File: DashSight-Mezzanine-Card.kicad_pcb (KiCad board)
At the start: 4 copper layers, 72 x 78.5 mm, 74 parts, among them IC2 ELM327, J1 Pi2 Connector, J2 Euler Connector, J3 Conn_Coaxial, J4 OBD2-DB9_Male, J5 Conn_02x05_Odd_Even, Q1 2N3904, Q2 2N3906, Q3 2N3906, Q4 2N3904, Q5 2N3904, Q6 2N3904, Q7 2N3904, SW1 SW_Push, SW2 SW_Push, U1 MCP2561-E/P, U2 LM317L_TO92, U3 LP2950-3.0_TO92, U4 ADuM1201AR, U5 NEO-M9N, Y1 4.0MHz

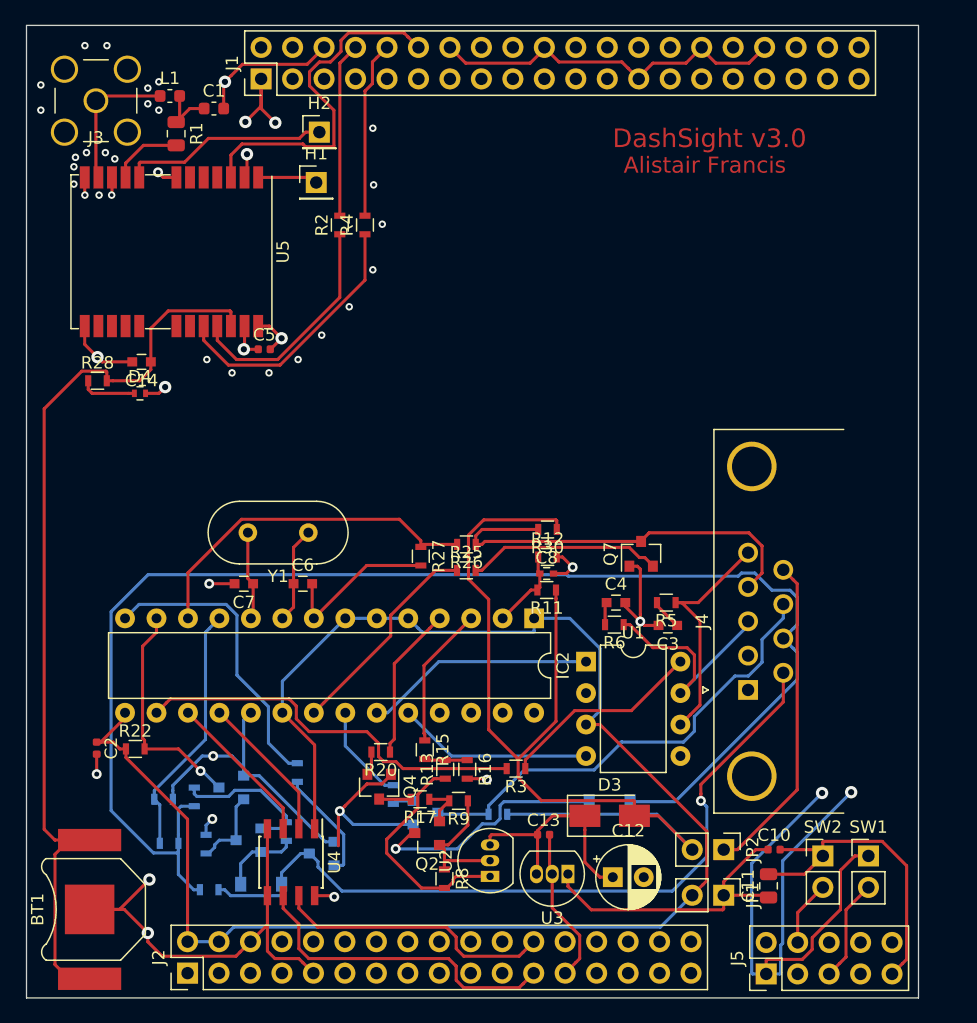
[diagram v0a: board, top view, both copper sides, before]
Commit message: pcb: Connect the IMU, GNSS PPS, Qwiic and other changes
Signed-off-by: Alistair Francis <alistair@alistair23.me>
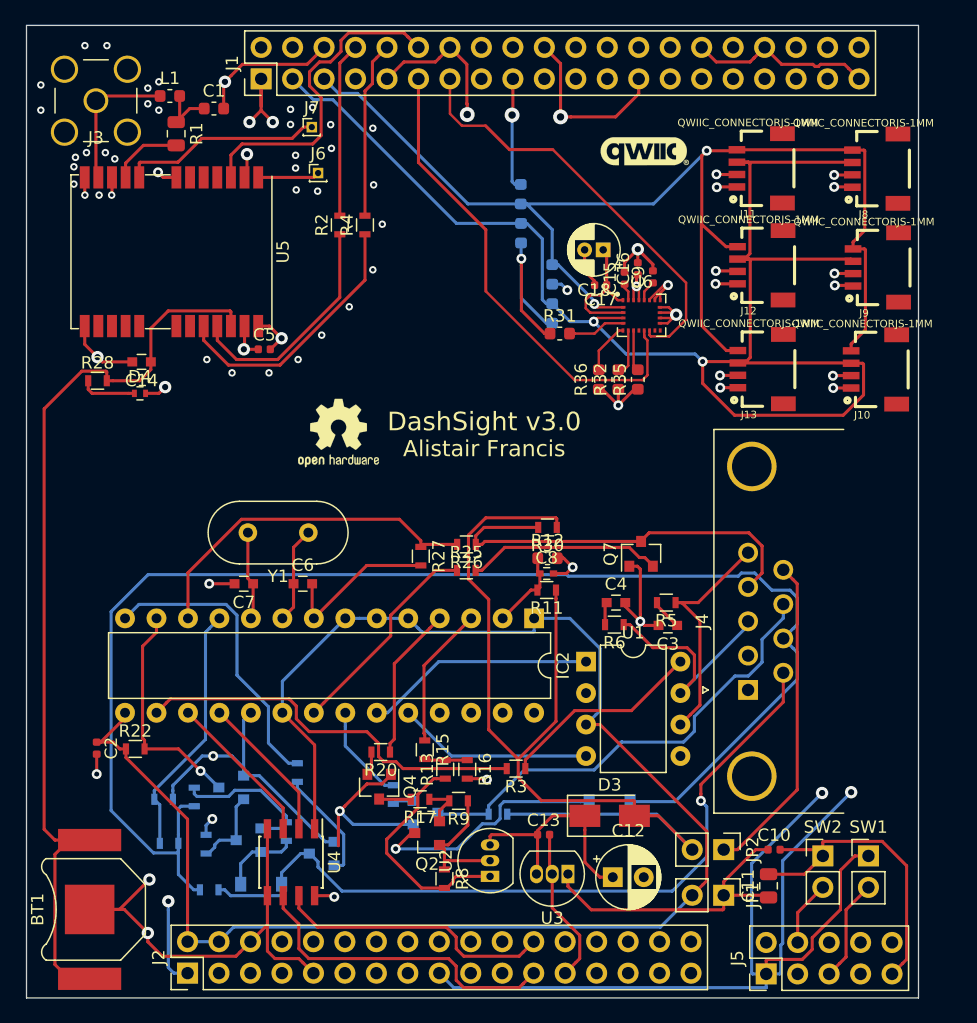
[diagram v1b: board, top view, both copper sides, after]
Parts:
- removed H1: Safeboot, Connector_PinHeader_2.54mm:PinHeader_1x01_P2.54mm_Vertical
- removed H2: Reset, Connector_PinHeader_2.54mm:PinHeader_1x01_P2.54mm_Vertical
- added C15: 0.1uF, Capacitor_SMD:C_0402_1005Metric, F.Cu at (176.3, 66.9)
- added C16: 0.1uF, Capacitor_SMD:C_0402_1005Metric, F.Cu at (177.3, 66.1)
- added C17: 0.1uF, Capacitor_SMD:C_0402_1005Metric, F.Cu at (174.3, 67.5)
- added C18: 10uF, Capacitor_THT:CP_Radial_D4.0mm_P1.50mm, F.Cu at (174.5, 64.6)
- added C9: 10nF (16V), Capacitor_SMD:C_0402_1005Metric, F.Cu at (178.6, 66.8)
- added G***: LOGO, DashSight:qwiic_logo, F.Cu at (177.9, 56.6)
- added J10: QWIIC_CONNECTORJS-1MM, DashSight:qwiic_connector, F.Cu at (194.6, 74.3)
- added J11: QWIIC_CONNECTORJS-1MM, DashSight:qwiic_connector, F.Cu at (185.3, 58.0)
- added J12: QWIIC_CONNECTORJS-1MM, DashSight:qwiic_connector, F.Cu at (185.4, 65.9)
- added J13: QWIIC_CONNECTORJS-1MM, DashSight:qwiic_connector, F.Cu at (185.4, 74.2)
- added J6: Safeboot, Connector_PinHeader_1.00mm:PinHeader_1x01_P1.00mm_Vertical, F.Cu at (151.5, 58.4)
- added J7: Reset, Connector_PinHeader_1.00mm:PinHeader_1x01_P1.00mm_Vertical, F.Cu at (151.0, 54.7)
- added J8: QWIIC_CONNECTORJS-1MM, DashSight:qwiic_connector, F.Cu at (194.7, 58.1)
- added J9: QWIIC_CONNECTORJS-1MM, DashSight:qwiic_connector, F.Cu at (194.7, 66.0)
- added R31: 10K, Resistor_SMD:R_0603_1608Metric, F.Cu at (171.0, 71.4)
- added R32: 10K, Resistor_SMD:R_0603_1608Metric, F.Cu at (175.8, 75.1)
- added R33: 10K, Resistor_SMD:R_0603_1608Metric, B.Cu at (170.4, 66.6)
- added R34: 10K, Resistor_SMD:R_0603_1608Metric, B.Cu at (170.4, 69.7)
- added R35: 10K, Resistor_SMD:R_0603_1608Metric, F.Cu at (177.3, 75.1)
- added R36: 10K, Resistor_SMD:R_0603_1608Metric, F.Cu at (174.2, 75.1)
- added R37: 2.2K, Resistor_SMD:R_0603_1608Metric, B.Cu at (167.9, 60.1)
- added R38: 2.2K, Resistor_SMD:R_0603_1608Metric, B.Cu at (167.9, 63.3)
- added REF**: OSHW-Logo2_7.3x6mm_SilkScreen, Symbol:OSHW-Logo2_7.3x6mm_SilkScreen, F.Cu at (153.2, 79.4)
- added U6: LSM9DS1, Package_LGA:LGA-24L_3x3.5mm_P0.43mm, F.Cu at (177.6, 69.9)
- R12: footprint Resistors_SMD:R_0603 -> Resistor_SMD:R_0603_1608Metric
- moved R30 0.17 mm to (170.1, 87.0)
- moved R12 0.10 mm to (170.1, 89.5)
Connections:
- J1 pad 11: (no net) -> PC7
- J1 pad 13: (no net) -> PH9
- J1 pad 17: (no net) -> +3V3
- J1 pad 3: (no net) -> I2C1_SDA
- J1 pad 5: (no net) -> I2C1_SCL
- J2 pad 1: (no net) -> +3V3
- J2 pad 17: (no net) -> +3V3
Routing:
- net I2C1_SDA: track 0.00 -> 118.3 mm, vias 0 -> 2
- net I2C1_SCL: track 0.00 -> 103.1 mm, vias 0 -> 2
- net +3V3: track 68.3 -> 157.7 mm, vias 8 -> 20
- net GND: track 202.8 -> 244.4 mm, vias 41 -> 61
- net PC7: track 0.00 -> 39.3 mm
- net PH9: track 0.00 -> 34.4 mm
- net Net-(R31-Pad2): track 0.00 -> 4.68 mm
- net Net-(R36-Pad2): track 0.00 -> 4.16 mm
- net Net-(R32-Pad2): track 0.00 -> 3.78 mm
- net Net-(R35-Pad2): track 0.00 -> 3.31 mm
- net PC8: track 28.5 -> 26.4 mm
- net Net-(C9-Pad1): track 0.00 -> 1.68 mm
- net Net-(C15-Pad1): track 0.00 -> 1.41 mm

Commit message: Breakout some GPIOs and fixup remaining issues
Signed-off-by: Alistair Francis <alistair@alistair23.me>
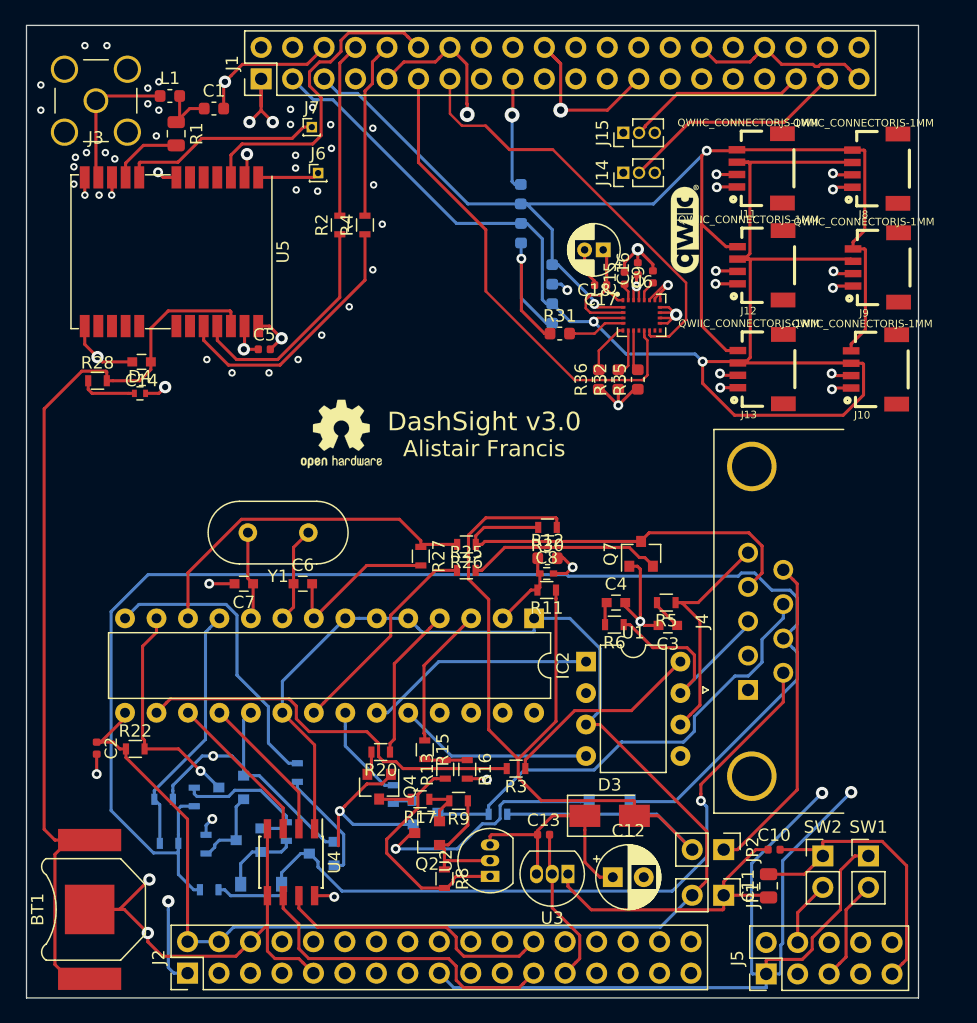
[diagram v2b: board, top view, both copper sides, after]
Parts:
- added J14: 1W-PC16, Connector_PinHeader_1.27mm:PinHeader_1x03_P1.27mm_Vertical, F.Cu at (176.2, 58.4)
- added J15: 1W-PC9, Connector_PinHeader_1.27mm:PinHeader_1x03_P1.27mm_Vertical, F.Cu at (176.2, 55.2)
- moved G*** 7.17 mm to (181.1, 63.0), turned to 90 degrees
- moved REF** 0.24 mm to (153.4, 79.5)
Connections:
- J1 pad 35: (no net) -> PC9
- J1 pad 37: (no net) -> PC16
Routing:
- net PC16: track 0.00 -> 18.4 mm
- net PC9: track 0.00 -> 14.5 mm
- net GND: track 244.4 -> 245.5 mm, vias 61 -> 62
- net +3V3: track 157.7 -> 158.3 mm

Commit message: pcb: Small corrections
Signed-off-by: Alistair Francis <alistair@alistair23.me>
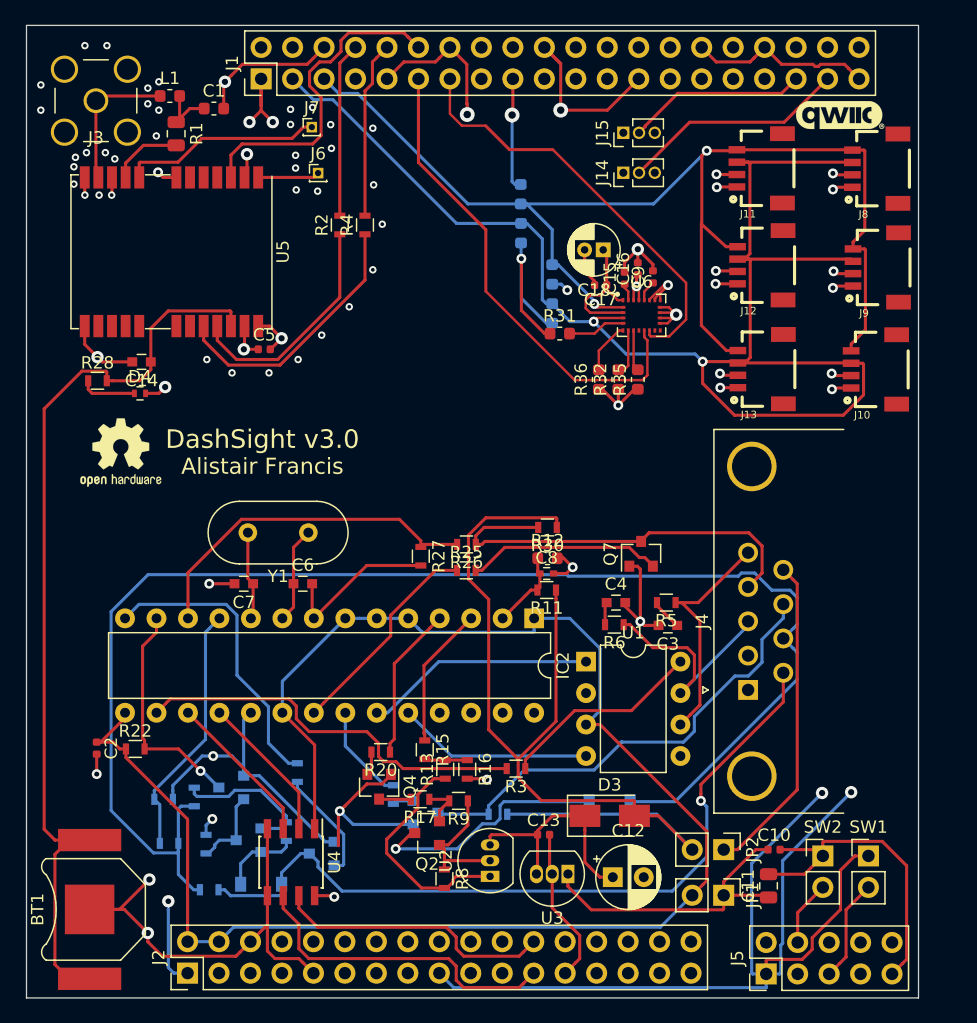
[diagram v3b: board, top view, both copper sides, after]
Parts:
- moved REF** 17.9 mm to (135.6, 81.0)
- moved G*** 15.6 mm to (193.6, 53.7), turned to 0 degrees
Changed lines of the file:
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@@
     (38 B.Mask user)
     (39 F.Mask user)
-    (40 Dwgs.User user)
-    (41 Cmts.User user)
-    (42 Eco1.User user)
+    (40 Dwgs.User user hide)
+    (41 Cmts.User user hide)
+    (42 Eco1.User user hide)
     (43 Eco2.User user)
     (44 Edge.Cuts user)
-    (45 Margin user)
+    (45 Margin user hide)
     (46 B.CrtYd user)
     (47 F.CrtYd user)
-    (48 B.Fab user)
-    (49 F.Fab user)
+    (48 B.Fab user hide)
+    (49 F.Fab user hide)
   )
   (setup
@@
     (visible_elements 7FFFFFFF)
     (pcbplotparams
-      (layerselection 0x010f0_ffffffff)
+      (layerselection 0x03fff_ffffffff)
       (usegerberextensions true)
       (usegerberattributes false)
@@
       (drillshape 0)
       (scaleselection 1)
-      (outputdirectory "PCB-Fabrication/v2.0-B/SeeedStudio/"))
+      (outputdirectory "PCB-Fabrication/v3.0/"))
   )
   (net 0 "")
@@
   )
   (module DashSight:qwiic_logo (layer F.Cu)
-    (at 181.0766 62.992 90)
-    (fp_text reference G*** (at 0 0 90) (layer F.SilkS) hide
+    (at 193.6242 53.6702)
+    (fp_text reference G*** (at 0 0) (layer F.SilkS) hide
       (effects (font (size 1.524 1.524) (thickness 0.3)))
     )
-    (fp_text value LOGO (at 0.75 0 90) (layer F.SilkS) hide
+    (fp_text value LOGO (at 0.75 0) (layer F.SilkS) hide
       (effects (font (size 1.524 1.524) (thickness 0.3)))
     )
@@
   )
   (module Symbol:OSHW-Logo2_7.3x6mm_SilkScreen (layer F.Cu)
-    (at 153.416 79.4766)
+    (at 135.6106 80.9752)
     (descr "Open Source Hardware Symbol")
     (tags "Logo Symbol OSHW")
@@
       (effects (font (size 0.6096 0.6096) (thickness 0.127)))
     )
-    (fp_text value QWIIC_CONNECTORJS-1MM (at 3.683 0.889) (layer F.SilkS)
+    (fp_text value QWIIC_CONNECTORJS-1MM (at 3.683 0.889) (layer F.SilkS) hide
       (effects (font (size 0.6096 0.6096) (thickness 0.127)))
     )
@@
       (effects (font (size 0.6096 0.6096) (thickness 0.127)))
     )
-    (fp_text value QWIIC_CONNECTORJS-1MM (at 3.683 0.889) (layer F.SilkS)
+    (fp_text value QWIIC_CONNECTORJS-1MM (at 3.683 0.889) (layer F.SilkS) hide
       (effects (font (size 0.6096 0.6096) (thickness 0.127)))
     )
@@
       (effects (font (size 0.6096 0.6096) (thickness 0.127)))
     )
-    (fp_text value QWIIC_CONNECTORJS-1MM (at 3.683 0.889) (layer F.SilkS)
+    (fp_text value QWIIC_CONNECTORJS-1MM (at 3.683 0.889) (layer F.SilkS) hide
       (effects (font (size 0.6096 0.6096) (thickness 0.127)))
     )
@@
       (effects (font (size 0.6096 0.6096) (thickness 0.127)))
     )
-    (fp_text value QWIIC_CONNECTORJS-1MM (at 3.683 0.889) (layer F.SilkS)
+    (fp_text value QWIIC_CONNECTORJS-1MM (at 3.683 0.889) (layer F.SilkS) hide
       (effects (font (size 0.6096 0.6096) (thickness 0.127)))
     )
@@
       (effects (font (size 0.6096 0.6096) (thickness 0.127)))
     )
-    (fp_text value QWIIC_CONNECTORJS-1MM (at 3.683 0.889) (layer F.SilkS)
+    (fp_text value QWIIC_CONNECTORJS-1MM (at 3.683 0.889) (layer F.SilkS) hide
       (effects (font (size 0.6096 0.6096) (thickness 0.127)))
     )
@@
       (effects (font (size 0.6096 0.6096) (thickness 0.127)))
     )
-    (fp_text value QWIIC_CONNECTORJS-1MM (at 3.683 0.889) (layer F.SilkS)
+    (fp_text value QWIIC_CONNECTORJS-1MM (at 3.683 0.889) (layer F.SilkS) hide
       (effects (font (size 0.6096 0.6096) (thickness 0.127)))
     )
@@
     )
   )
-  (gr_text "Alistair Francis" (at 164.9476 80.6704) (layer F.SilkS)
+  (gr_text "Alistair Francis" (at 147.0406 82.0928) (layer F.SilkS)
     (effects (font (size 1.3 1.3) (thickness 0.3)))
   )
-  (gr_text "DashSight v3.0" (at 164.9476 78.486) (layer F.SilkS)
+  (gr_text "DashSight v3.0" (at 147.0406 79.9084) (layer F.SilkS)
     (effects (font (size 1.5 1.5) (thickness 0.3)))
   )

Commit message: Only support 6 Qwiic connections
I was worried I couuldn't fit the cables in with 6

Signed-off-by: Alistair Francis <alistair@alistair23.me>
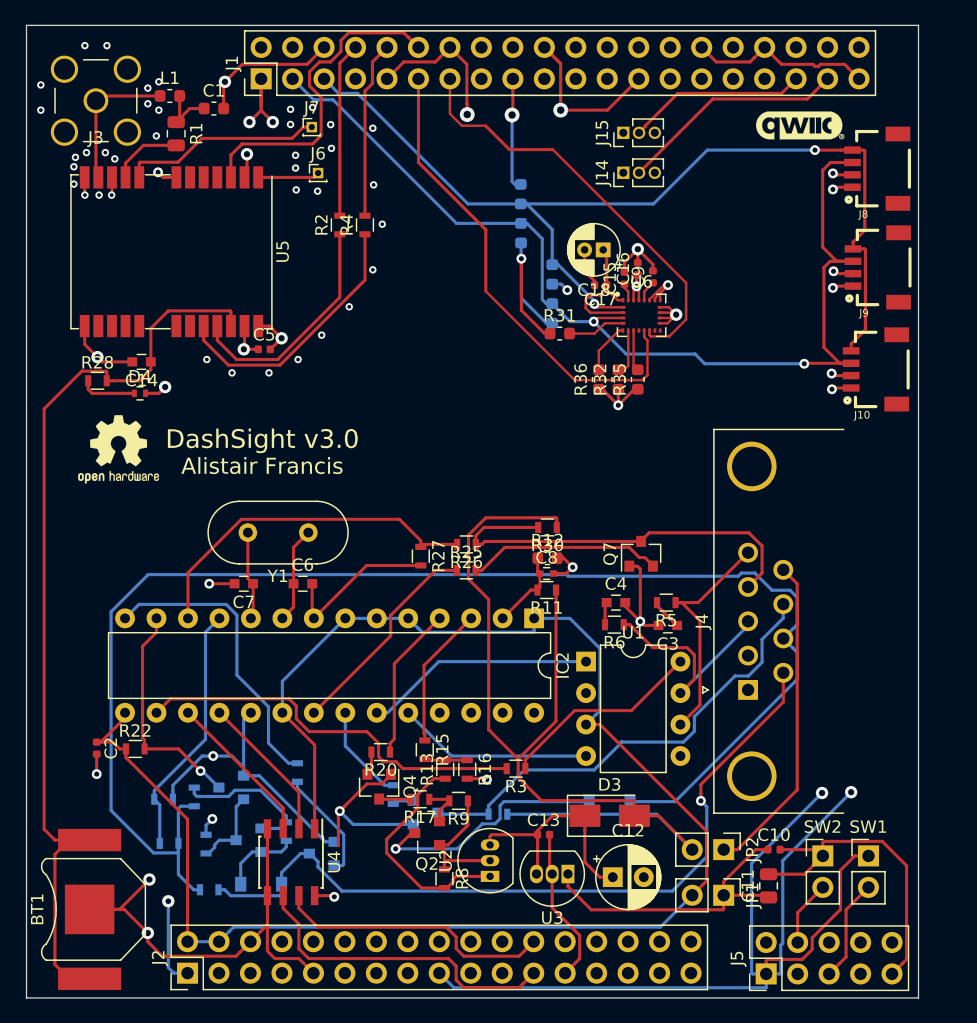
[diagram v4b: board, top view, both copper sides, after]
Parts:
- removed J11, J12, J13: QWIIC_CONNECTORJS-1MM, DashSight:qwiic_connector
- moved G*** 3.33 mm to (190.4, 54.5)
- moved REF** 0.31 mm to (135.4, 80.7)
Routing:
- net I2C1_SDA: track 118.3 -> 83.9 mm
- net I2C1_SCL: track 103.1 -> 81.4 mm
- net +3V3: track 158.3 -> 153.2 mm, vias 20 -> 17
- net GND: track 245.5 -> 240.6 mm, vias 62 -> 59

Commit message: pcb: Update some of the footprints
Signed-off-by: Alistair Francis <alistair@alistair23.me>
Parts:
- J1: footprint Pin_Headers:Pin_Header_Straight_2x20_Pitch2.54mm -> Connector_PinSocket_2.54mm:PinSocket_2x20_P2.54mm_Vertical; moved to B.Cu
- J2: footprint Pin_Headers:Pin_Header_Straight_2x17_Pitch2.54mm -> Connector_PinSocket_2.54mm:PinSocket_2x17_P2.54mm_Vertical; moved to B.Cu
- J3: footprint Connectors:SMA_THT_Jack_Straight -> Connector_Coaxial:SMA_Amphenol_132134_Vertical
- J5: footprint Connector_PinHeader_2.54mm:PinHeader_2x05_P2.54mm_Vertical -> Connector_PinSocket_2.54mm:PinSocket_2x05_P2.54mm_Vertical; moved to B.Cu
- JP1, JP2: footprint Pin_Headers:Pin_Header_Straight_1x02_Pitch2.54mm -> Connector_PinHeader_2.54mm:PinHeader_1x02_P2.54mm_Vertical
- U1: footprint Housings_DIP:DIP-8_W7.62mm -> Package_DIP:DIP-8_W7.62mm
- U2: footprint TO_SOT_Packages_THT:TO-92_Inline_Narrow_Oval -> Package_TO_SOT_THT:TO-92_Inline
- U4: footprint Housings_SOIC:SOIC-8_3.9x4.9mm_Pitch1.27mm -> Package_SO:SOIC-8_3.9x4.9mm_P1.27mm
- Y1: footprint Crystals:Crystal_HC49-U_Vertical -> Crystal:Crystal_HC49-U_Vertical
- turned J1 to 270 degrees
- turned J2 to 270 degrees
- turned J5 to 270 degrees
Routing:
- net GND: vias 59 -> 58
- net (no net): vias 0 -> 1
